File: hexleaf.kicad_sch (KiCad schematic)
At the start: 53 parts, among them IC1 ESP32-C3-FH4, IC2 MAX14781EESA+, J1 009155005201006, J2 Conn_01x04, J3 009155005201006, J5 Conn_01x08, J6 Conn_01x04, J7 Conn_01x08, SW1 SW_SPST, SW2 SW_SPST, Y1 ECS-400-10-37B2-CKM-TR

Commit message: started layout
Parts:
- J6: footprint (none) -> hexleaf:WS2815_Strip_4P_Full
- R12, R13: footprint Resistor_SMD:R_0805_2012Metric -> Resistor_SMD:R_0402_1005Metric
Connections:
- net GPIO16 is gone; now on net EDGE0: IC1.23 (SPID)
- net GPIO17 is gone; now on net EDGE1: IC1.24 (SPIQ)
- net EDGE0: no longer IC1.4 (XTAL_32K_P)
- net EDGE1: no longer IC1.5 (XTAL_32K_N)
- new net GPIO0: IC1.4 (XTAL_32K_P)
- new net GPIO1: IC1.5 (XTAL_32K_N)
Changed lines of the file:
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@@
     )
   )
-  (global_label "EDGE1" (shape input) (at 259.08 86.36 180) (fields_autoplaced)
-    (effects (font (size 1.27 1.27)) (justify right))
-    (property "Intersheet References" "${INTERSHEET_REFS}" (id 0) (at 250.7082 86.2806 0)
-      (effects (font (size 1.27 1.27)) (justify right) hide)
+  (global_label "EDGE1" (shape input) (at 326.39 86.36 0) (fields_autoplaced)
+    (effects (font (size 1.27 1.27)) (justify left))
+    (property "Intersheet References" "${INTERSHEET_REFS}" (id 0) (at 334.7618 86.4394 0)
+      (effects (font (size 1.27 1.27)) (justify left) hide)
     )
   )
@@
     )
   )
-  (global_label "EDGE0" (shape input) (at 259.08 83.82 180) (fields_autoplaced)
-    (effects (font (size 1.27 1.27)) (justify right))
-    (property "Intersheet References" "${INTERSHEET_REFS}" (id 0) (at 250.7082 83.7406 0)
-      (effects (font (size 1.27 1.27)) (justify right) hide)
+  (global_label "EDGE0" (shape input) (at 326.39 88.9 0) (fields_autoplaced)
+    (effects (font (size 1.27 1.27)) (justify left))
+    (property "Intersheet References" "${INTERSHEET_REFS}" (id 0) (at 334.7618 88.9794 0)
+      (effects (font (size 1.27 1.27)) (justify left) hide)
     )
   )
@@
     (property "Reference" "R13" (id 0) (at 382.27 59.69 0))
     (property "Value" "10k" (id 1) (at 382.27 62.23 0))
-    (property "Footprint" "Resistor_SMD:R_0805_2012Metric" (id 2) (at 378.46 60.96 0)
+    (property "Footprint" "Resistor_SMD:R_0402_1005Metric" (id 2) (at 378.46 60.96 0)
       (effects (font (size 1.27 1.27)) hide)
     )
@@
       (effects (font (size 1.27 1.27)) (justify left))
     )
-    (property "Footprint" "" (id 2) (at 106.68 149.86 0)
+    (property "Footprint" "hexleaf:WS2815_Strip_4P_Full" (id 2) (at 106.68 149.86 0)
       (effects (font (size 1.27 1.27)) hide)
     )
@@
     (property "Datasheet" "~" (id 3) (at 284.48 157.48 0)
       (effects (font (size 1.27 1.27)) hide)
+    )
+    (pin "1")
+    (pin "2")
+  )
+  (symbol (lib_id "Device:R_Small") (at 378.46 40.64 180) (unit 1)
+    (in_bom yes) (on_board yes)
+    (property "Reference" "R12" (id 0) (at 382.27 39.37 0))
+    (property "Value" "10k" (id 1) (at 382.27 41.91 0))
+    (property "Footprint" "Resistor_SMD:R_0402_1005Metric" (id 2) (at 378.46 40.64 0)
+      (effects (font (size 1.27 1.27)) hide)
+    )
+    (property "Datasheet" "https://www.mouser.de/datasheet/2/447/PYu_RC_Group_51_RoHS_L_10-1664068.pdf" (id 3) (at 378.46 40.64 0)
+      (effects (font (size 1.27 1.27)) hide)
+    )
+    (property "MFN" " 603-RC0402FR-0710KL " (id 4) (at 378.46 40.64 0)
+      (effects (font (size 1.27 1.27)) hide)
+    )
+    (property "in stock" "b." (id 5) (at 377.19 40.64 0)
+      (effects (font (size 1.27 1.27)) (justify left))
     )
     (pin "1")
@@
     (pin "2")
   )
-  (symbol (lib_id "Device:R_Small") (at 378.46 40.64 180) (unit 1)
-    (in_bom yes) (on_board yes)
-    (property "Reference" "R12" (id 0) (at 382.27 39.37 0))
-    (property "Value" "10k" (id 1) (at 382.27 41.91 0))
-    (property "Footprint" "Resistor_SMD:R_0805_2012Metric" (id 2) (at 378.46 40.64 0)
-      (effects (font (size 1.27 1.27)) hide)
-    )
-    (property "Datasheet" "https://www.mouser.de/datasheet/2/447/PYu_RC_Group_51_RoHS_L_10-1664068.pdf" (id 3) (at 378.46 40.64 0)
-      (effects (font (size 1.27 1.27)) hide)
-    )
-    (property "MFN" " 603-RC0402FR-0710KL " (id 4) (at 378.46 40.64 0)
-      (effects (font (size 1.27 1.27)) hide)
-    )
-    (property "in stock" "b." (id 5) (at 377.19 40.64 0)
-      (effects (font (size 1.27 1.27)) (justify left))
-    )
-    (pin "1")
-    (pin "2")
-  )
   (symbol (lib_id "Jumper:SolderJumper_2_Open") (at 57.15 152.4 90) (unit 1)
     (in_bom yes) (on_board yes)
@@
     )
     (path "/16e7f86d-2283-4e9b-86c9-30f5f38f682b"
-      (reference "J6") (unit 1) (value "Conn_01x04") (footprint "")
+      (reference "J6") (unit 1) (value "Conn_01x04") (footprint "hexleaf:WS2815_Strip_4P_Full")
     )
     (path "/28d5f755-ae65-42a6-882e-df3c414cf483"
@@
       (reference "R11") (unit 1) (value "470R") (footprint "Resistor_SMD:R_0402_1005Metric")
     )
-    (path "/eb0bb8bc-b294-4a58-a337-95a413bdd34a"
-      (reference "R12") (unit 1) (value "10k") (footprint "Resistor_SMD:R_0805_2012Metric")
+    (path "/8208a877-1896-47c5-b498-a9a96b7a0534"
+      (reference "R12") (unit 1) (value "10k") (footprint "Resistor_SMD:R_0402_1005Metric")
     )
     (path "/0a517b9a-a9fc-44f0-b6e1-5b5bad5d4c74"
-      (reference "R13") (unit 1) (value "10k") (footprint "Resistor_SMD:R_0805_2012Metric")
+      (reference "R13") (unit 1) (value "10k") (footprint "Resistor_SMD:R_0402_1005Metric")
     )
     (path "/508cc352-4d19-4358-95ba-715645cd1a5a"

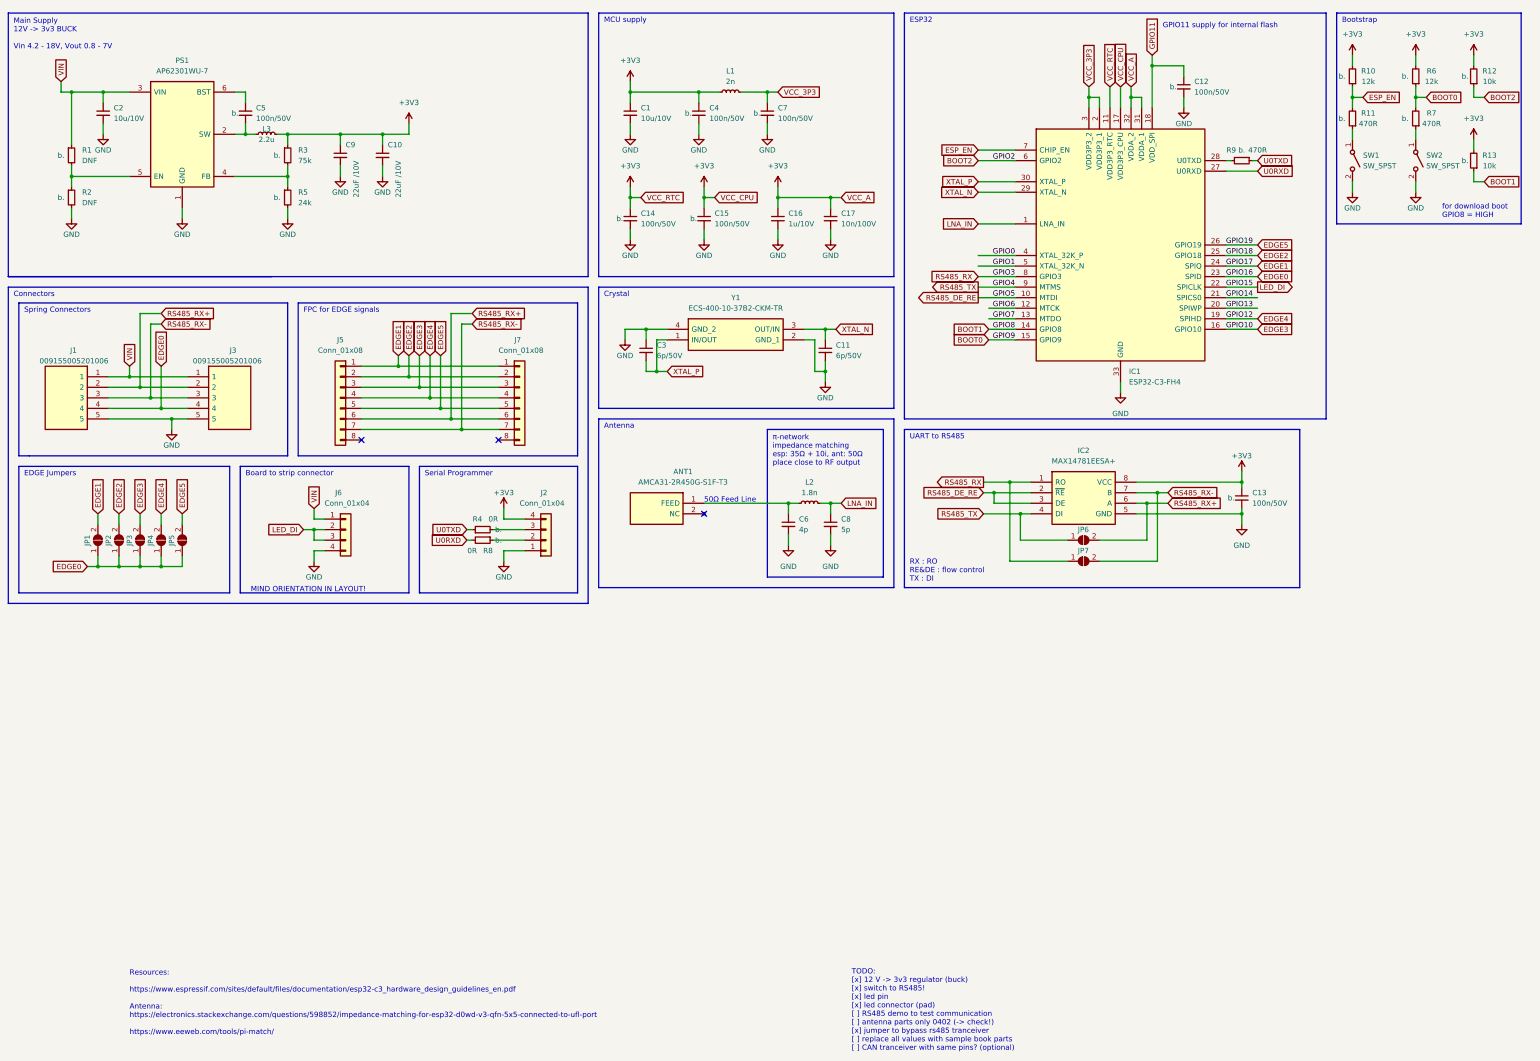
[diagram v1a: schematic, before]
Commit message: updated schematic (crystal symbol)
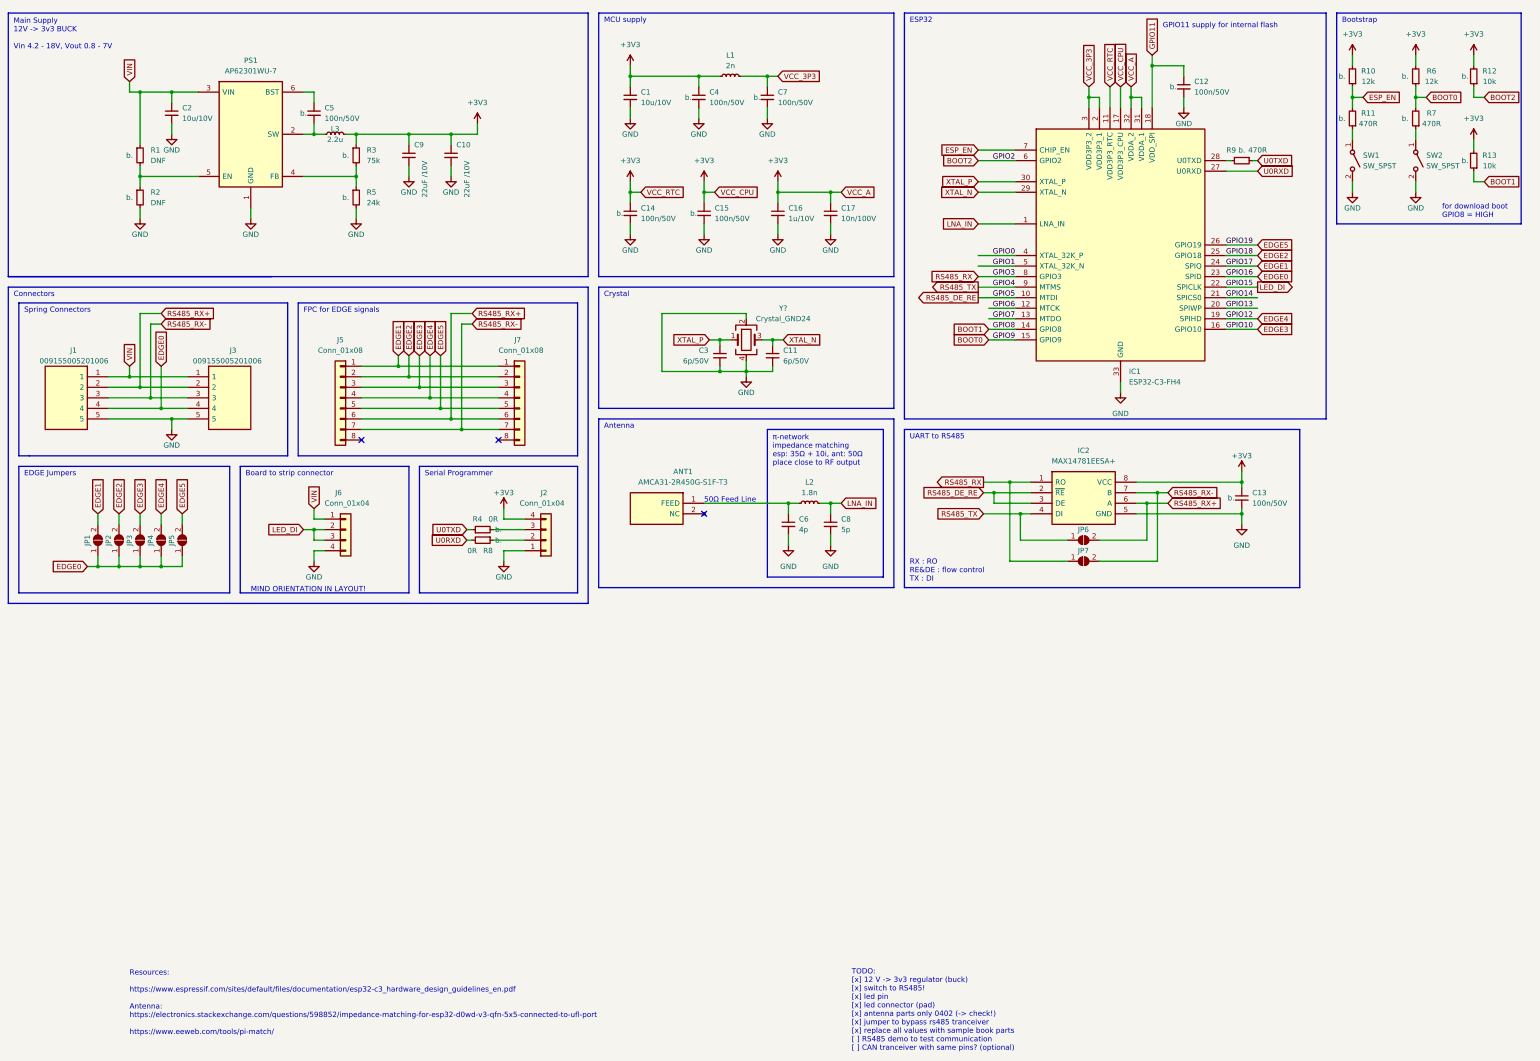
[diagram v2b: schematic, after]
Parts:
- removed Y1: ECS-400-10-37B2-CKM-TR, hexleaf:ECS4001037B2CKMTR, symbol hexleaf:ECS-400-10-37B2-CKM-TR
- added Y?: Crystal_GND24, hexleaf:ECS4001037B2CKMTR, symbol Device:Crystal_GND24
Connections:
- net GND: now also C3.2, Y?.2, Y?.4; no longer C3.1
- net XTAL_N: now also Y?.3
- net XTAL_P: now also C3.1, Y?.1; no longer C3.2
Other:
- note added: "TODO: [x] 12 V -> 3v3 regulator (buck) [x] switch to RS485! [x] led pin [x] led connector (pad) [x] antenna parts only 0402 (-> check!) [x] jumper to bypass rs485 tranceiver [x] replace all values with sample book parts [ ] RS485 demo to test communication [ ] CAN tranceiver with same pins? (optional)"
- note removed: "TODO: [x] 12 V -> 3v3 regulator (buck) [x] switch to RS485! [x] led pin [x] led connector (pad) [ ] RS485 demo to test communication [ ] antenna parts only 0402 (-> check!) [x] jumper to bypass rs485 tranceiver [ ] replace all values with sample book parts [ ] CAN tranceiver with same pins? (optional)"
- moved on the sheet: C1, C10, C11, C14, C15, C16, C17, C2, C3, C4, C5, C7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
